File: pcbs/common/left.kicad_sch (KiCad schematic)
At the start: 89 parts, among them J2 TRS

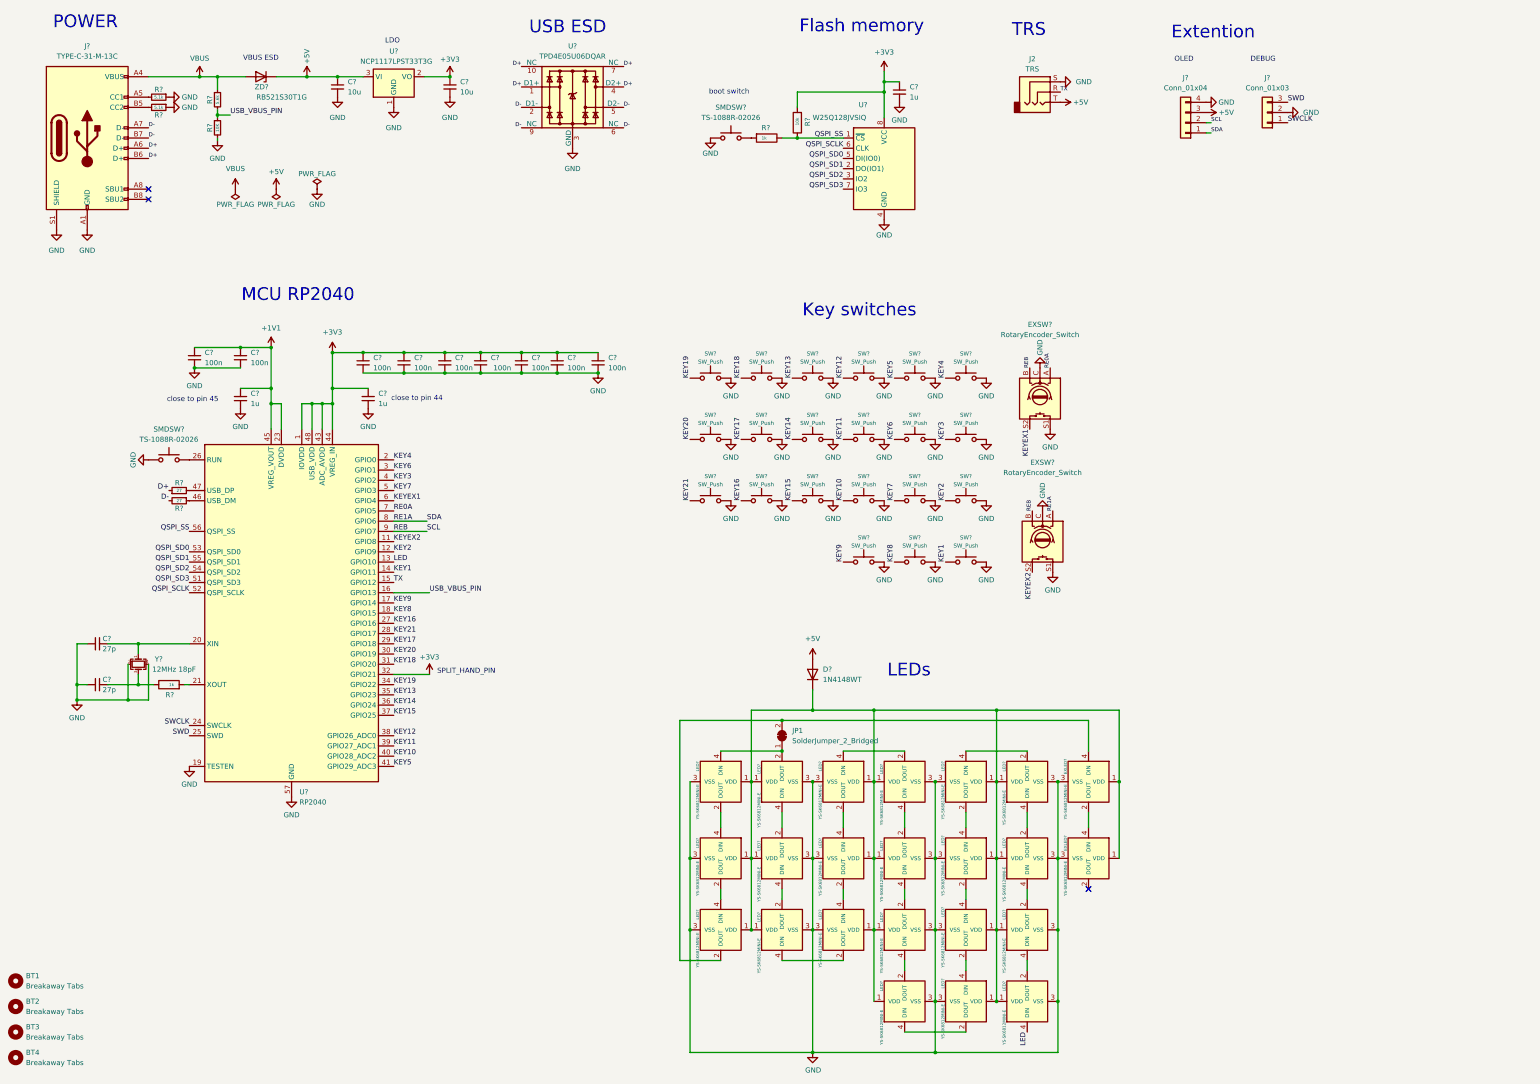
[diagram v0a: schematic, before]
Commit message: Split comms through USB-C. Added more ESD.
Made a switch from TRS to USB-C for better ESD and short-circuit prevention. Added ferrite beads on external connections.
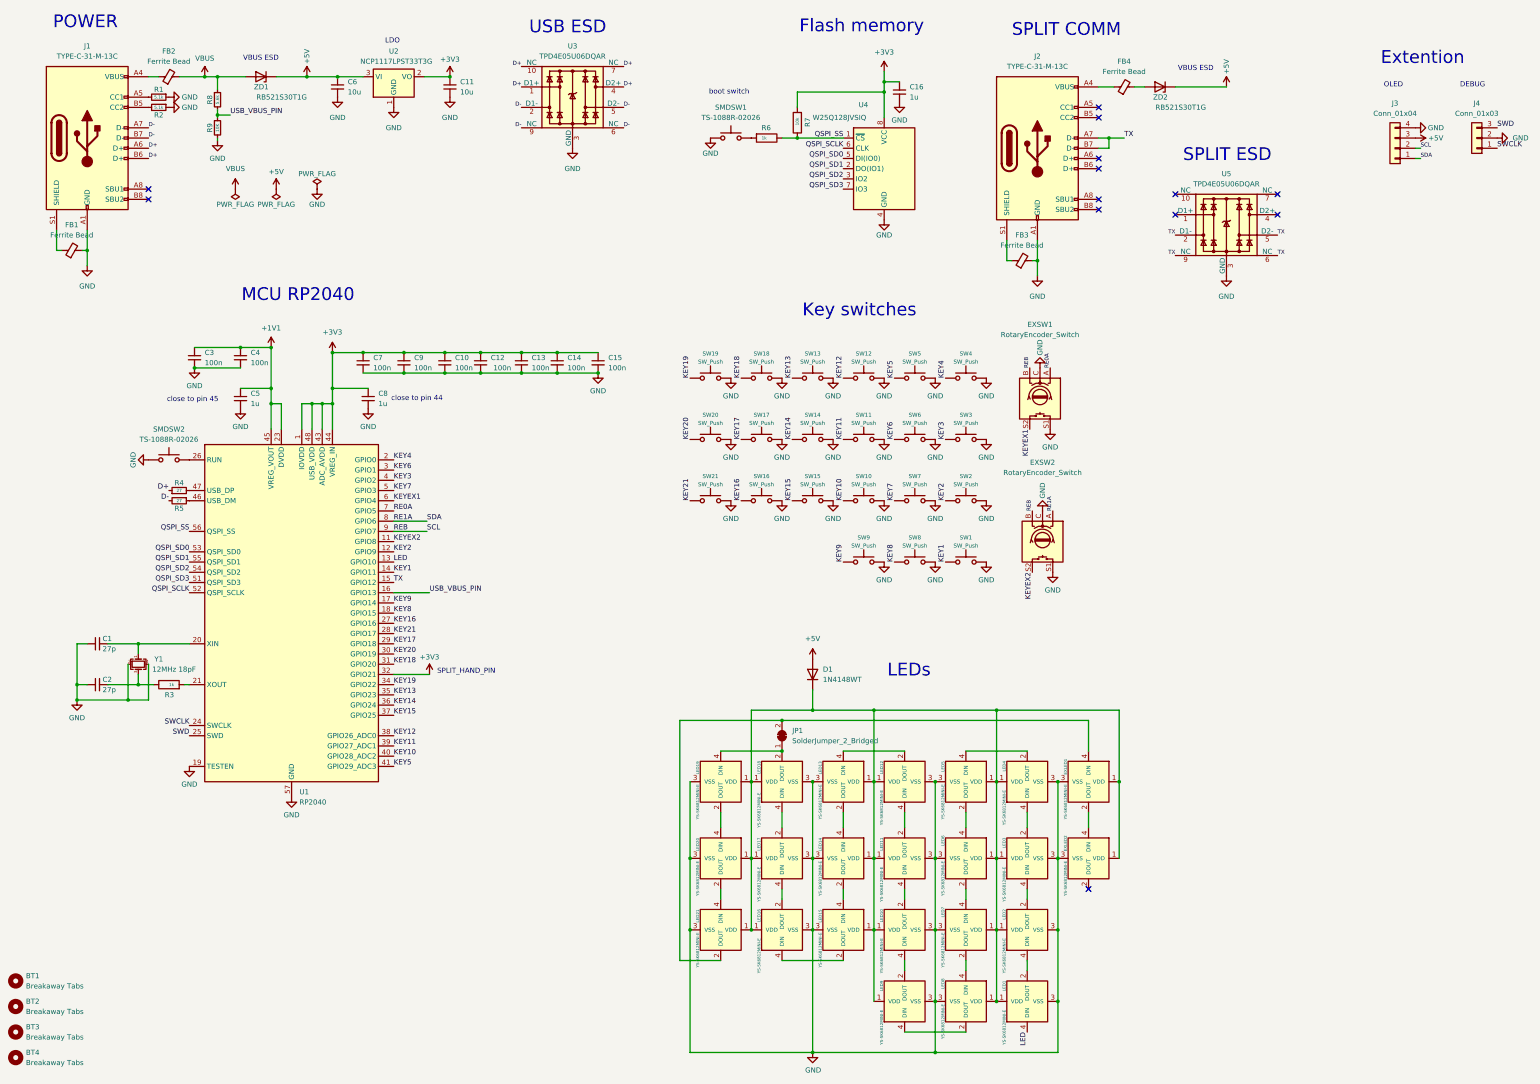
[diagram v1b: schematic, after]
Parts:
- removed J2: TRS, kbd_local:PJ-398A-5A_PJ-399B-6A, symbol Connector_Audio:AudioJack3
- added FB1, FB2, FB3, FB4: Ferrite Bead, Capacitor_SMD:C_0603_1608Metric_Pad1.08x0.95mm_HandSolder, symbol Device:FerriteBead_Small
- added J2: TYPE-C-31-M-13C, kbd_local:TYPE-C-31-M-13C, symbol kbd_local:USB_C_Receptacle_USB2.0_16P
- added U5: TPD4E05U06DQAR, Package_SON:USON-10_2.5x1.0mm_P0.5mm, symbol Power_Protection:TPD4EUSB30
- added ZD2: RB521S30T1G, Diode_SMD:D_SOD-523, symbol Diode:ESD5Zxx
- J1: renamed from J?; symbol Connector:USB_C_Receptacle_USB2.0 -> kbd_local:USB_C_Receptacle_USB2.0_16P
- gave numbers to parts that had none: 82
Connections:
- net +5V: now also ZD2.1 (K)
- net GND: now also FB1.2, FB3.2, J2.A1 (GND), J2.B1 (GND), U5.3 (GND), U5.8 (GND); no longer J1.A12 (GND), J1.B12 (GND), J1.S1 (SHIELD)
- net TX: now also J2.A7 (D-), J2.B7 (D-), U5.2 (D1-), U5.5 (D2-), U5.6 (NC), U5.9 (NC)
- net VBUS: now also FB2.2; no longer J1.A4 (VBUS), J1.A9 (VBUS), J1.B4 (VBUS), J1.B9 (VBUS)
- new net: FB3.1, J2.S1 (SHIELD)
- new net: FB4.2, ZD2.2 (A)
- new net: FB4.1, J2.A4 (VBUS), J2.B4 (VBUS)
- new net: FB2.1, J1.A4 (VBUS), J1.B4 (VBUS)
- new net: FB1.1, J1.S1 (SHIELD)
- no-connect marks 3 -> 13
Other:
- note added: "SPLIT COMM"
- note added: "SPLIT ESD"
- note removed: "TRS"
- moved on the sheet: J3, J4

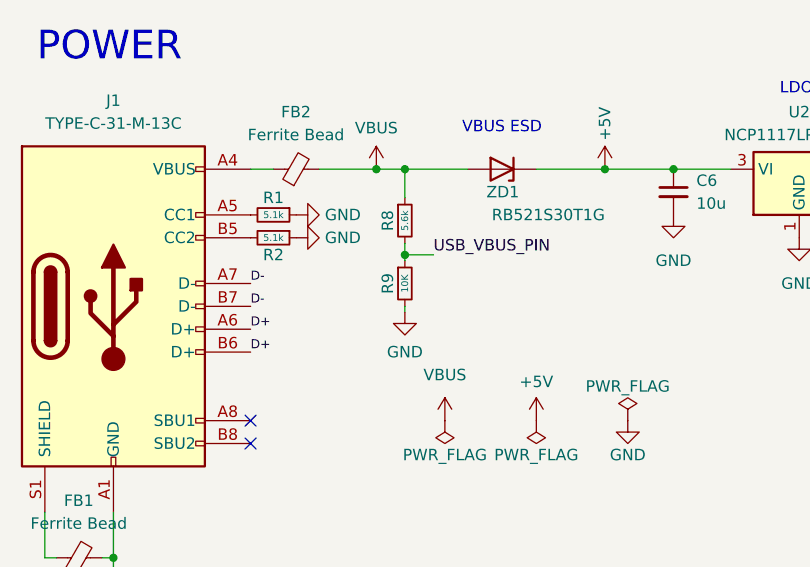
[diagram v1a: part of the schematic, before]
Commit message: fixes and preparing for pcba
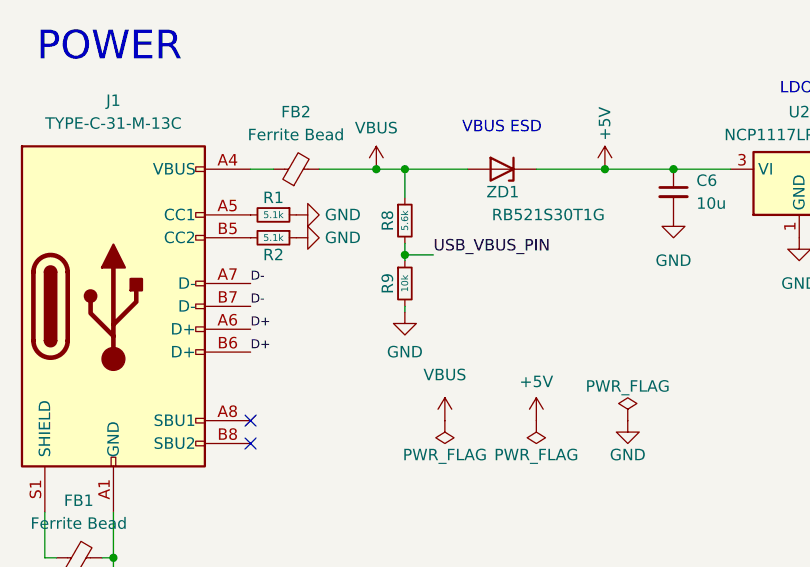
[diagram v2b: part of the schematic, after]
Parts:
- C1, C2: LSCS Part # (none) -> C1557
- C10, C12, C13, C14, C15, C3, C4, C7, C9: LSCS Part # (none) -> C1525
- C11, C6: LSCS Part # (none) -> C15525
- C16, C5, C8: LSCS Part # (none) -> C52923
- D1: JLCPCB Part # C232841 -> (none); LSCS Part # (none) -> C232841
- EXLED1, EXLED2, LED1, LED10, LED11, LED12, LED13, LED14, LED15, LED16, LED17, LED18, LED19, LED2, LED20, LED21, LED3, LED4, LED5, LED6, LED7, LED8, LED9: LSCS Part # (none) -> C5149201
- FB1, FB2, FB3, FB4: JLCPCB Part # C882974 -> (none); LSCS Part # (none) -> C882974
- J1, J2: JLCPCB Part # C2848620 -> (none); LSCS Part # (none) -> C2848620
- R1, R2: LSCS Part # (none) -> C25905
- R3, R6: LSCS Part # (none) -> C11702
- R4, R5: LSCS Part # (none) -> C25100
- R7: LSCS Part # (none) -> C25744
- R8: LSCS Part # (none) -> C25908
- R9: value 10K -> 10k; LSCS Part # (none) -> C25744
- SMDSW1, SMDSW2: JLCPCB Part # C455280 -> (none); LSCS Part # (none) -> C455280
- U1: JLCPCB Part # C2040 -> (none); LSCS Part # (none) -> C2040
- U2: JLCPCB Part # C146799 -> (none); LSCS Part # (none) -> C146799
- U3, U5: JLCPCB Part # C138714 -> (none); LSCS Part # (none) -> C138714
- U4: JLCPCB Part # C113767 -> (none); LSCS Part # (none) -> C113767
- Y1: JLCPCB Part # C91749 -> (none); LSCS Part # (none) -> C91749
- ZD1, ZD2: JLCPCB Part # C145179 -> (none); LSCS Part # (none) -> C145179
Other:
- company: foostan -> tomislavrekic

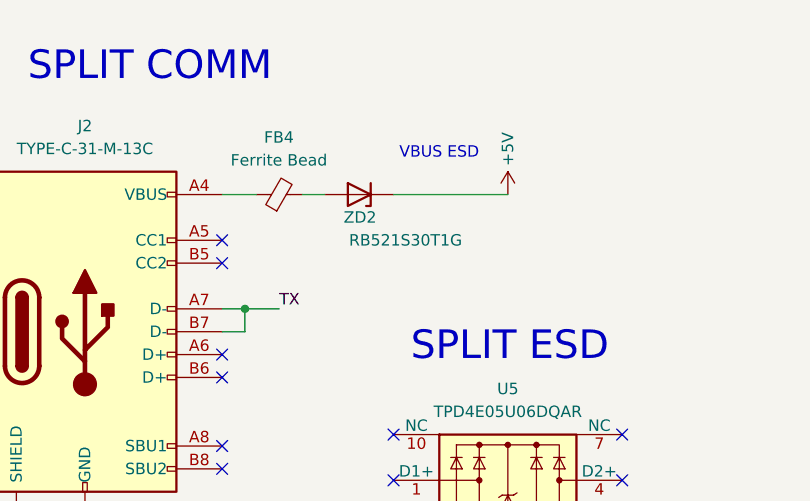
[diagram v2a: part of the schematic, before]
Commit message: Removed diode on split USB
The diode blocked power to the other half of the keyboard.
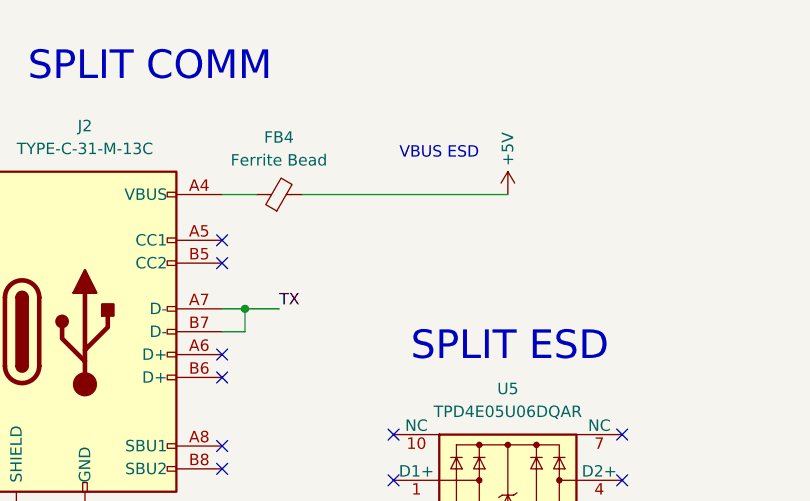
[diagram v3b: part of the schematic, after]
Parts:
- removed ZD2: RB521S30T1G, Diode_SMD:D_SOD-523, symbol Diode:ESD5Zxx
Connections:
- net +5V: now also FB4.2
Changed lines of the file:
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@@
 	(wire
 		(pts
-			(xy 306.07 35.56) (xy 318.77 35.56)
-		)
-		(stroke
-			(width 0)
-			(type default)
-		)
-	)
-	(wire
-		(pts
 			(xy 50.8 187.96) (xy 45.72 187.96)
 		)
@@
 	(wire
 		(pts
-			(xy 295.91 35.56) (xy 298.45 35.56)
+			(xy 295.91 35.56) (xy 318.77 35.56)
 		)
 		(stroke
@@
 					(unit 1)
 				)
-			)
-		)
-	)
-	(symbol
-		(lib_id "Diode:ESD5Zxx")
-		(at 302.26 35.56 180)
-		(unit 1)
-		(exclude_from_sim no)
-		(in_bom yes)
-		(on_board yes)
-		(dnp no)
-		(property "Reference" "ZD2"
-			(at 304.165 38.1 0)
-			(effects
-				(font
-					(size 1.27 1.27)
-				)
-				(justify left)
-			)
-		)
-		(property "Value" "RB521S30T1G"
-			(at 313.69 40.64 0)
-			(effects
-				(font
-					(size 1.27 1.27)
-				)
-				(justify left)
-			)
-		)
-		(property "Footprint" "Diode_SMD:D_SOD-523"
-			(at 302.26 31.115 0)
-			(effects
-				(font
-					(size 1.27 1.27)
-				)
-				(hide yes)
-			)
-		)
-		(property "Datasheet" ""
-			(at 302.26 35.56 0)
-			(effects
-				(font
-					(size 1.27 1.27)
-				)
-				(hide yes)
-			)
-		)
-		(property "Description" ""
-			(at 302.26 35.56 0)
-			(effects
-				(font
-					(size 1.27 1.27)
-				)
-				(hide yes)
-			)
-		)
-		(property "LSCS Part #" "C145179"
-			(at 302.26 35.56 0)
-			(effects
-				(font
-					(size 1.27 1.27)
-				)
-				(hide yes)
-			)
-		)
-		(pin "1"
-		)
-		(pin "2"
-		)
-		(instances
-			(project "corne-cherry"
-				(path "/4cc5d416-57f5-4147-8183-e03ae6b1198a/089db7cd-2934-428b-a62a-55e0735649ba"
-					(reference "ZD2")
-					(unit 1)
-				)
-			)
-			(project "left"
-				(path "/5d636ecb-124e-4eb3-8682-4273aa9c70aa"
-					(reference "ZD?")
-					(unit 1)
-				)
